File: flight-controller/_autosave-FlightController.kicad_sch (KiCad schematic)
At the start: 38 parts, among them J1 MSD-4-A, J2 Conn_01x03_Pin, J3 Conn_01x03_Pin, J4 Conn_01x03_Pin, J5 Conn_01x03_Pin, J6 USB4215-03-A_REVA, J7 Conn_01x03_Pin, J8 Conn_01x03_Pin, J9 Conn_01x04_Pin, U1 ESP32-S3-WROOM-1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

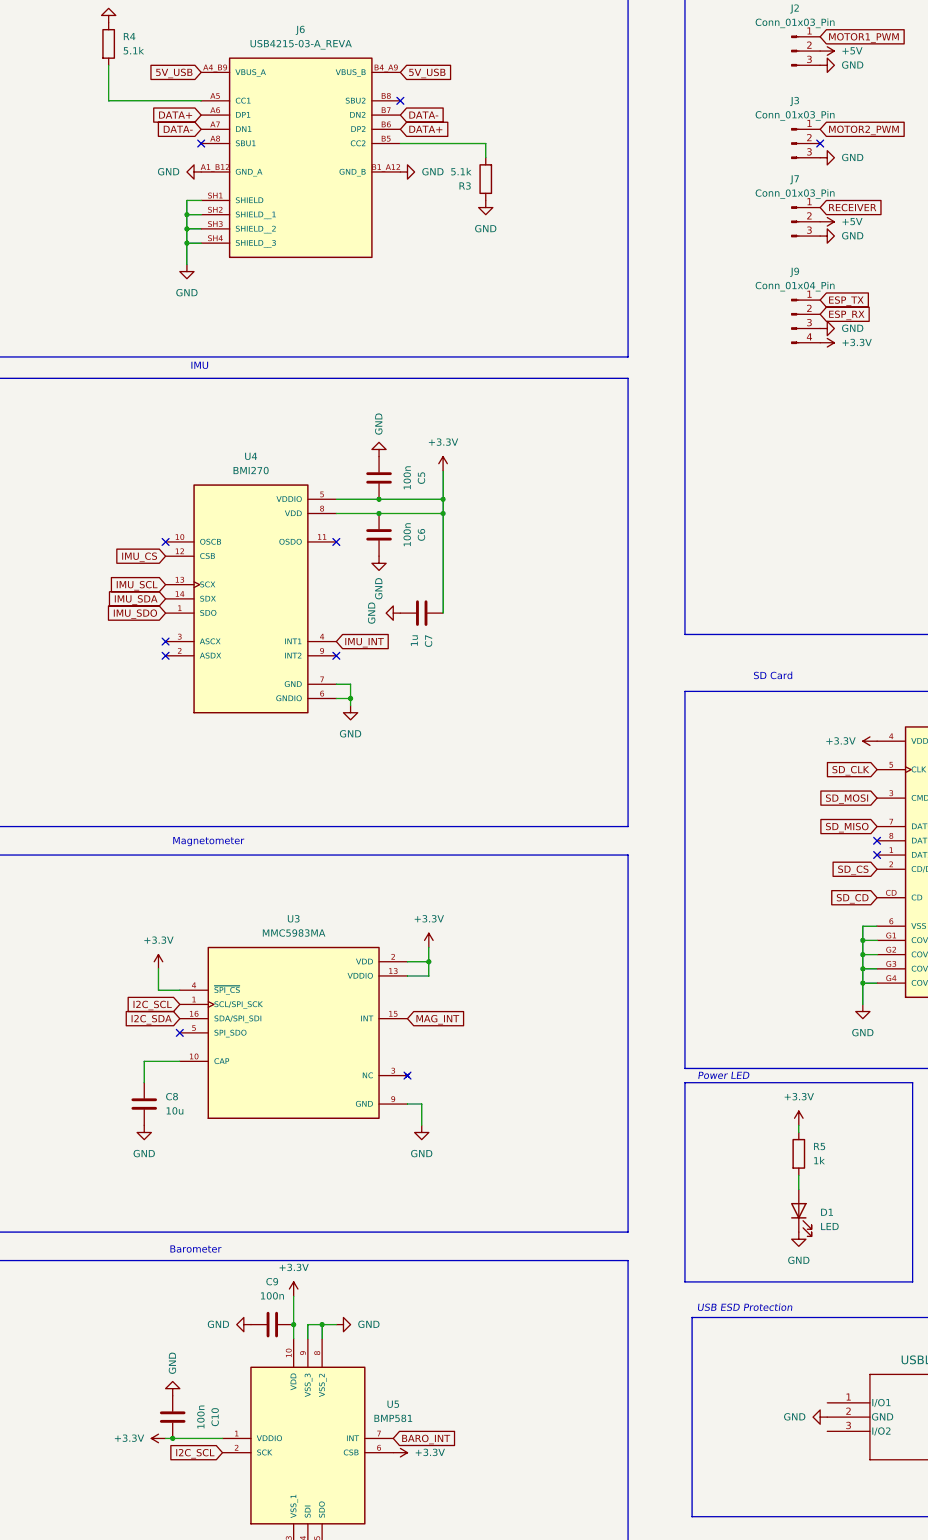
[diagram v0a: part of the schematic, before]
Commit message: esd protection
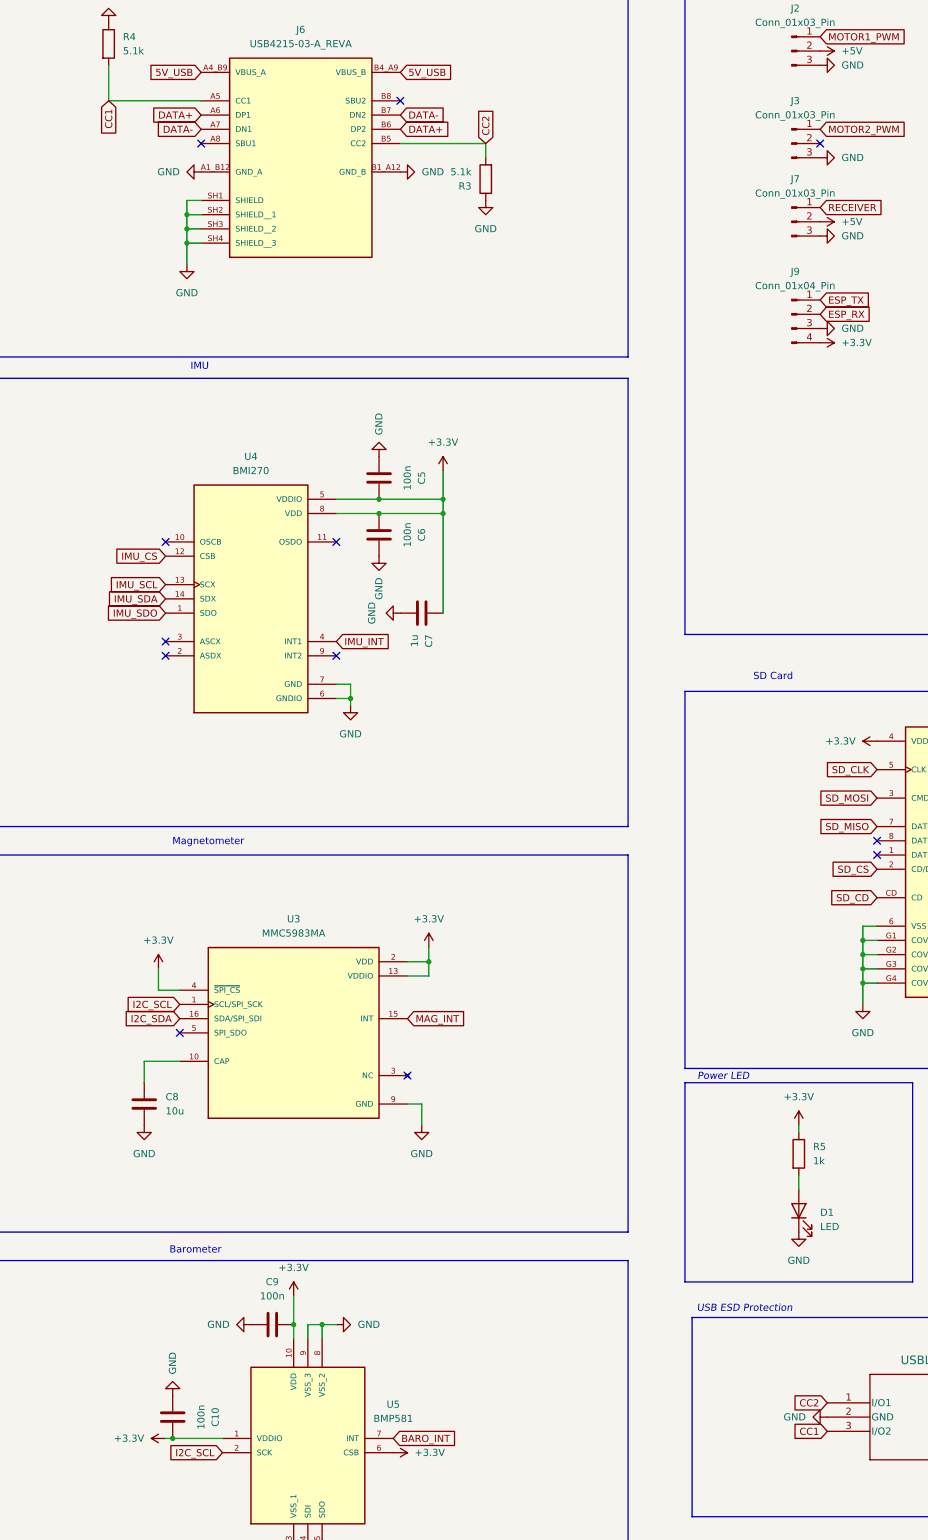
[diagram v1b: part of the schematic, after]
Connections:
- net CC2: now reaches CR1.1 (I/O1)
- net CC2: now also J6.B5 (CC2), R3.2
- net CC1: now reaches CR1.3 (I/O2)
- net CC1: now also J6.A5 (CC1), R4.2
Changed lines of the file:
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@@
+		)
+	)
+	(global_label "CC2"
+		(shape input)
+		(at 110.49 140.97 90)
+		(fields_autoplaced yes)
+		(effects
+			(font
+				(size 1.27 1.27)
+			)
+			(justify left)
+		)
+		(property "Intersheetrefs" "${INTERSHEET_REFS}"
+			(at 110.49 134.2353 90)
+			(effects
+				(font
+					(size 1.27 1.27)
+				)
+				(justify left)
+				(hide yes)
+			)
 		)
 	)
@@
 		)
 	)
+	(global_label "CC2"
+		(shape input)
+		(at 171.45 365.76 180)
+		(fields_autoplaced yes)
+		(effects
+			(font
+				(size 1.27 1.27)
+			)
+			(justify right)
+		)
+		(property "Intersheetrefs" "${INTERSHEET_REFS}"
+			(at 164.7153 365.76 0)
+			(effects
+				(font
+					(size 1.27 1.27)
+				)
+				(justify right)
+				(hide yes)
+			)
+		)
+	)
 	(global_label "SD_MISO"
 		(shape input)
@@
 		)
 	)
+	(global_label "CC1"
+		(shape input)
+		(at 171.45 370.84 180)
+		(fields_autoplaced yes)
+		(effects
+			(font
+				(size 1.27 1.27)
+			)
+			(justify right)
+		)
+		(property "Intersheetrefs" "${INTERSHEET_REFS}"
+			(at 164.7153 370.84 0)
+			(effects
+				(font
+					(size 1.27 1.27)
+				)
+				(justify right)
+				(hide yes)
+			)
+		)
+	)
 	(global_label "ESP_RX"
 		(shape input)
@@
 				(hide yes)
 			)
+		)
+	)
+	(global_label "CC1"
+		(shape input)
+		(at 43.18 133.35 270)
+		(fields_autoplaced yes)
+		(effects
+			(font
+				(size 1.27 1.27)
+			)
+			(justify right)
+		)
+		(property "Intersheetrefs" "${INTERSHEET_REFS}"
+			(at 43.18 140.0847 90)
+			(effects
+				(font
+					(size 1.27 1.27)
+				)
+				(justify right)
+				(hide yes)
+			)
